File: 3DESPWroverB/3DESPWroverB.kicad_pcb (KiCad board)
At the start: 2 copper layers, 40 x 40 mm, 18 parts, among them J1 Conn_02x07_Odd_Even, J10 Conn_02x03_Odd_Even, J11 Conn_01x01, J12 Conn_01x01, J13 Conn_01x01, J14 Conn_01x01, J15 Conn_01x01, J16 Conn_01x01, J17 Conn_01x01, J18 Conn_01x01, J2 Conn_01x01, J3 Conn_01x01, J4 Conn_01x01, J5 Conn_01x01, J6 Conn_01x01, J7 Conn_01x01, J8 Conn_01x01, J9 Conn_01x01

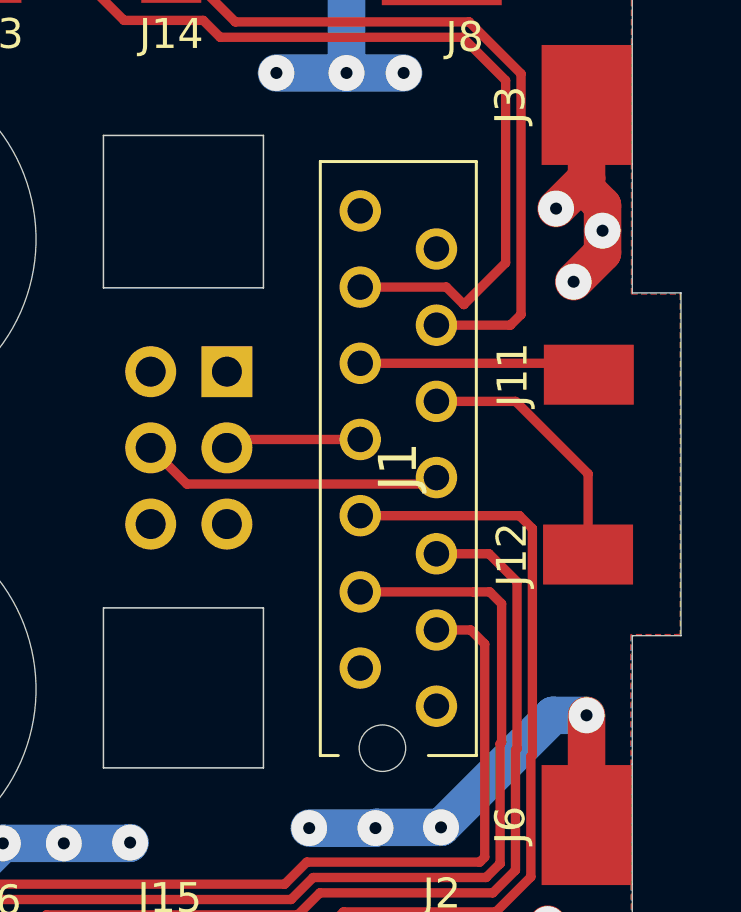
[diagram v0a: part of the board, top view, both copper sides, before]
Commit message: Correction to 3.3v regulator connection
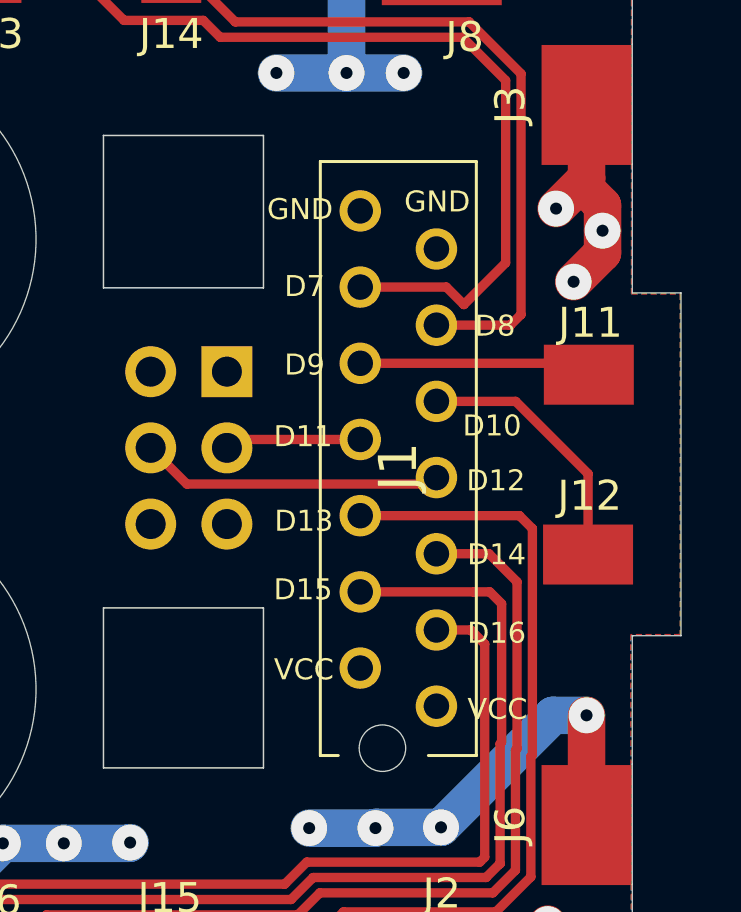
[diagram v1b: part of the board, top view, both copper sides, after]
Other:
- board text added: "D10"
- board text added: "D11"
- board text added: "D12"
- board text added: "D13"
- board text added: "D14"
- board text added: "D15"
- board text added: "D16"
- board text added: "D7"
- board text added: "D8"
- board text added: "D9"
- board text added: "GND"
- board text added: "VCC"
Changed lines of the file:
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@@
   (general
     (thickness 1.6)
-    (drawings 105)
+    (drawings 125)
     (tracks 138)
     (zones 0)
@@
       (effects (font (size 1.27 1.27) (thickness 0.254)))
     )
+    (fp_line (start -1.645 -3.87) (end 18.155 -3.87) (layer F.Fab) (width 0.2))
+    (fp_line (start 18.155 -3.87) (end 18.155 1.33) (layer F.Fab) (width 0.2))
+    (fp_line (start 18.155 1.33) (end -1.645 1.33) (layer F.Fab) (width 0.2))
+    (fp_line (start -1.645 1.33) (end -1.645 -3.87) (layer F.Fab) (width 0.2))
+    (fp_line (start -2.645 -4.87) (end 19.685 -4.87) (layer F.CrtYd) (width 0.1))
+    (fp_line (start 19.685 -4.87) (end 19.685 2.33) (layer F.CrtYd) (width 0.1))
+    (fp_line (start 19.685 2.33) (end -2.645 2.33) (layer F.CrtYd) (width 0.1))
+    (fp_line (start -2.645 2.33) (end -2.645 -4.87) (layer F.CrtYd) (width 0.1))
+    (fp_line (start 18.155 -2.27) (end 18.155 -3.87) (layer F.SilkS) (width 0.1))
+    (fp_line (start 18.155 -3.87) (end -1.645 -3.87) (layer F.SilkS) (width 0.1))
+    (fp_line (start -1.645 -3.87) (end -1.645 1.33) (layer F.SilkS) (width 0.1))
+    (fp_line (start -1.645 1.33) (end 18.155 1.33) (layer F.SilkS) (width 0.1))
     (fp_line (start 18.155 1.33) (end 18.155 0.73) (layer F.SilkS) (width 0.1))
-    (fp_line (start -1.645 1.33) (end 18.155 1.33) (layer F.SilkS) (width 0.1))
-    (fp_line (start -1.645 -3.87) (end -1.645 1.33) (layer F.SilkS) (width 0.1))
-    (fp_line (start 18.155 -3.87) (end -1.645 -3.87) (layer F.SilkS) (width 0.1))
-    (fp_line (start 18.155 -2.27) (end 18.155 -3.87) (layer F.SilkS) (width 0.1))
-    (fp_line (start -2.645 2.33) (end -2.645 -4.87) (layer F.CrtYd) (width 0.1))
-    (fp_line (start 19.685 2.33) (end -2.645 2.33) (layer F.CrtYd) (width 0.1))
-    (fp_line (start 19.685 -4.87) (end 19.685 2.33) (layer F.CrtYd) (width 0.1))
-    (fp_line (start -2.645 -4.87) (end 19.685 -4.87) (layer F.CrtYd) (width 0.1))
-    (fp_line (start -1.645 1.33) (end -1.645 -3.87) (layer F.Fab) (width 0.2))
-    (fp_line (start 18.155 1.33) (end -1.645 1.33) (layer F.Fab) (width 0.2))
-    (fp_line (start 18.155 -3.87) (end 18.155 1.33) (layer F.Fab) (width 0.2))
-    (fp_line (start -1.645 -3.87) (end 18.155 -3.87) (layer F.Fab) (width 0.2))
     (fp_text user %R (at 8.52 -1.27 90) (layer F.Fab)
       (effects (font (size 1.27 1.27) (thickness 0.254)))
@@
   (module Custom:CubeCenterPad (layer F.Cu)
     (at 168.6052 54.4576 270)
-    (fp_text reference J11 (at 0 2.54 90) (layer F.SilkS)
+    (fp_text reference J11 (at -1.7272 -0.0508 180) (layer F.SilkS)
       (effects (font (size 1 1) (thickness 0.15)))
     )
@@
   (module Custom:CubeCenterPad (layer F.Cu)
     (at 168.5798 60.452 270)
-    (fp_text reference J12 (at 0 2.54 90) (layer F.SilkS)
+    (fp_text reference J12 (at -1.9558 -0.0508 180) (layer F.SilkS)
       (effects (font (size 1 1) (thickness 0.15)))
     )
@@
     (descr "Through hole straight pin header, 2x03, 2.54mm pitch, double rows")
     (tags "Through hole pin header THT 2x03 2.54mm double row")
-    (fp_text reference J10 (at 5.2578 -0.8128) (layer B.SilkS)
+    (fp_text reference J10 (at 5.3086 -1.3208) (layer B.SilkS)
       (effects (font (size 1 1) (thickness 0.15)) (justify mirror))
     )
@@
       (effects (font (size 1 1) (thickness 0.15)) (justify mirror))
     )
+    (fp_line (start 0 1.27) (end 3.81 1.27) (layer B.Fab) (width 0.1))
+    (fp_line (start 3.81 1.27) (end 3.81 -6.35) (layer B.Fab) (width 0.1))
+    (fp_line (start 3.81 -6.35) (end -1.27 -6.35) (layer B.Fab) (width 0.1))
+    (fp_line (start -1.27 -6.35) (end -1.27 0) (layer B.Fab) (width 0.1))
+    (fp_line (start -1.27 0) (end 0 1.27) (layer B.Fab) (width 0.1))
+    (fp_line (start -1.33 -6.41) (end 3.87 -6.41) (layer B.SilkS) (width 0.12))
+    (fp_line (start -1.33 -1.27) (end -1.33 -6.41) (layer B.SilkS) (width 0.12))
+    (fp_line (start 3.87 1.33) (end 3.87 -6.41) (layer B.SilkS) (width 0.12))
+    (fp_line (start -1.33 -1.27) (end 1.27 -1.27) (layer B.SilkS) (width 0.12))
+    (fp_line (start 1.27 -1.27) (end 1.27 1.33) (layer B.SilkS) (width 0.12))
+    (fp_line (start 1.27 1.33) (end 3.87 1.33) (layer B.SilkS) (width 0.12))
+    (fp_line (start -1.33 0) (end -1.33 1.33) (layer B.SilkS) (width 0.12))
+    (fp_line (start -1.33 1.33) (end 0 1.33) (layer B.SilkS) (width 0.12))
+    (fp_line (start -1.8 1.8) (end -1.8 -6.85) (layer B.CrtYd) (width 0.05))
+    (fp_line (start -1.8 -6.85) (end 4.35 -6.85) (layer B.CrtYd) (width 0.05))
+    (fp_line (start 4.35 -6.85) (end 4.35 1.8) (layer B.CrtYd) (width 0.05))
     (fp_line (start 4.35 1.8) (end -1.8 1.8) (layer B.CrtYd) (width 0.05))
-    (fp_line (start 4.35 -6.85) (end 4.35 1.8) (layer B.CrtYd) (width 0.05))
-    (fp_line (start -1.8 -6.85) (end 4.35 -6.85) (layer B.CrtYd) (width 0.05))
-    (fp_line (start -1.8 1.8) (end -1.8 -6.85) (layer B.CrtYd) (width 0.05))
-    (fp_line (start -1.33 1.33) (end 0 1.33) (layer B.SilkS) (width 0.12))
-    (fp_line (start -1.33 0) (end -1.33 1.33) (layer B.SilkS) (width 0.12))
-    (fp_line (start 1.27 1.33) (end 3.87 1.33) (layer B.SilkS) (width 0.12))
-    (fp_line (start 1.27 -1.27) (end 1.27 1.33) (layer B.SilkS) (width 0.12))
-    (fp_line (start -1.33 -1.27) (end 1.27 -1.27) (layer B.SilkS) (width 0.12))
-    (fp_line (start 3.87 1.33) (end 3.87 -6.41) (layer B.SilkS) (width 0.12))
-    (fp_line (start -1.33 -1.27) (end -1.33 -6.41) (layer B.SilkS) (width 0.12))
-    (fp_line (start -1.33 -6.41) (end 3.87 -6.41) (layer B.SilkS) (width 0.12))
-    (fp_line (start -1.27 0) (end 0 1.27) (layer B.Fab) (width 0.1))
-    (fp_line (start -1.27 -6.35) (end -1.27 0) (layer B.Fab) (width 0.1))
-    (fp_line (start 3.81 -6.35) (end -1.27 -6.35) (layer B.Fab) (width 0.1))
-    (fp_line (start 3.81 1.27) (end 3.81 -6.35) (layer B.Fab) (width 0.1))
-    (fp_line (start 0 1.27) (end 3.81 1.27) (layer B.Fab) (width 0.1))
     (fp_text user %R (at 1.27 -2.54 270) (layer B.Fab)
       (effects (font (size 1 1) (thickness 0.15)) (justify mirror))
@@
     )
   )
+  (gr_text GND (at 151.5618 54.229 180) (layer B.SilkS)
+    (effects (font (size 0.7 0.7) (thickness 0.15)) (justify mirror))
+  )
+  (gr_text GND (at 163.5506 48.6918) (layer F.SilkS)
+    (effects (font (size 0.7 0.7) (thickness 0.15)))
+  )
+  (gr_text GND (at 158.9786 48.9458) (layer F.SilkS)
+    (effects (font (size 0.7 0.7) (thickness 0.15)))
+  )
+  (gr_text VCC (at 165.5572 65.6082) (layer F.SilkS)
+    (effects (font (size 0.7 0.7) (thickness 0.15)))
+  )
+  (gr_text VCC (at 159.1056 64.2874) (layer F.SilkS)
+    (effects (font (size 0.7 0.7) (thickness 0.15)))
+  )
+  (gr_text D16 (at 165.5318 63.0682) (layer F.SilkS)
+    (effects (font (size 0.7 0.7) (thickness 0.15)))
+  )
+  (gr_text D15 (at 159.0802 61.6204) (layer F.SilkS)
+    (effects (font (size 0.7 0.7) (thickness 0.15)))
+  )
+  (gr_text D14 (at 165.5318 60.452) (layer F.SilkS)
+    (effects (font (size 0.7 0.7) (thickness 0.15)))
+  )
+  (gr_text D13 (at 159.1056 59.3344) (layer F.SilkS)
+    (effects (font (size 0.7 0.7) (thickness 0.15)))
+  )
+  (gr_text D12 (at 165.5064 57.9882) (layer F.SilkS)
+    (effects (font (size 0.7 0.7) (thickness 0.15)))
+  )
+  (gr_text D11 (at 159.0802 56.515) (layer F.SilkS)
+    (effects (font (size 0.7 0.7) (thickness 0.15)))
+  )
+  (gr_text D10 (at 165.3794 56.1594) (layer F.SilkS)
+    (effects (font (size 0.7 0.7) (thickness 0.15)))
+  )
+  (gr_text D9 (at 159.131 54.1274) (layer F.SilkS)
+    (effects (font (size 0.7 0.7) (thickness 0.15)))
+  )
+  (gr_text D8 (at 165.481 52.832) (layer F.SilkS)
+    (effects (font (size 0.7 0.7) (thickness 0.15)))
+  )
+  (gr_text D7 (at 159.131 51.5112) (layer F.SilkS)
+    (effects (font (size 0.7 0.7) (thickness 0.15)))
+  )
+  (gr_text D11 (at 158.7246 56.8452 180) (layer B.SilkS)
+    (effects (font (size 0.7 0.7) (thickness 0.15)) (justify mirror))
+  )
+  (gr_text D12 (at 151.3332 57.023 180) (layer B.SilkS)
+    (effects (font (size 0.7 0.7) (thickness 0.15)) (justify mirror))
+  )
+  (gr_text VCC (at 156.591 61.2648 180) (layer B.SilkS)
+    (effects (font (size 0.7 0.7) (thickness 0.15)) (justify mirror))
+  )
+  (gr_text VCC (at 156.5656 52.4002 180) (layer B.SilkS)
+    (effects (font (size 0.7 0.7) (thickness 0.15)) (justify mirror))
+  )
+  (gr_text GND (at 151.257 59.5884 180) (layer B.SilkS)
+    (effects (font (size 0.7 0.7) (thickness 0.15)) (justify mirror))
+  )
   (gr_text "REAL\nITU\nrodr" (at 151.6888 42.2656) (layer B.SilkS)
     (effects (font (size 1 1) (thickness 0.15)) (justify mirror))
   )
-  (gr_text "Project Cube, v1.1" (at 144.5768 57.4802) (layer B.SilkS)
+  (gr_text "Project Cube, v1.1" (at 142.0114 57.4548) (layer B.SilkS)
     (effects (font (size 1 1) (thickness 0.15)) (justify mirror))
   )

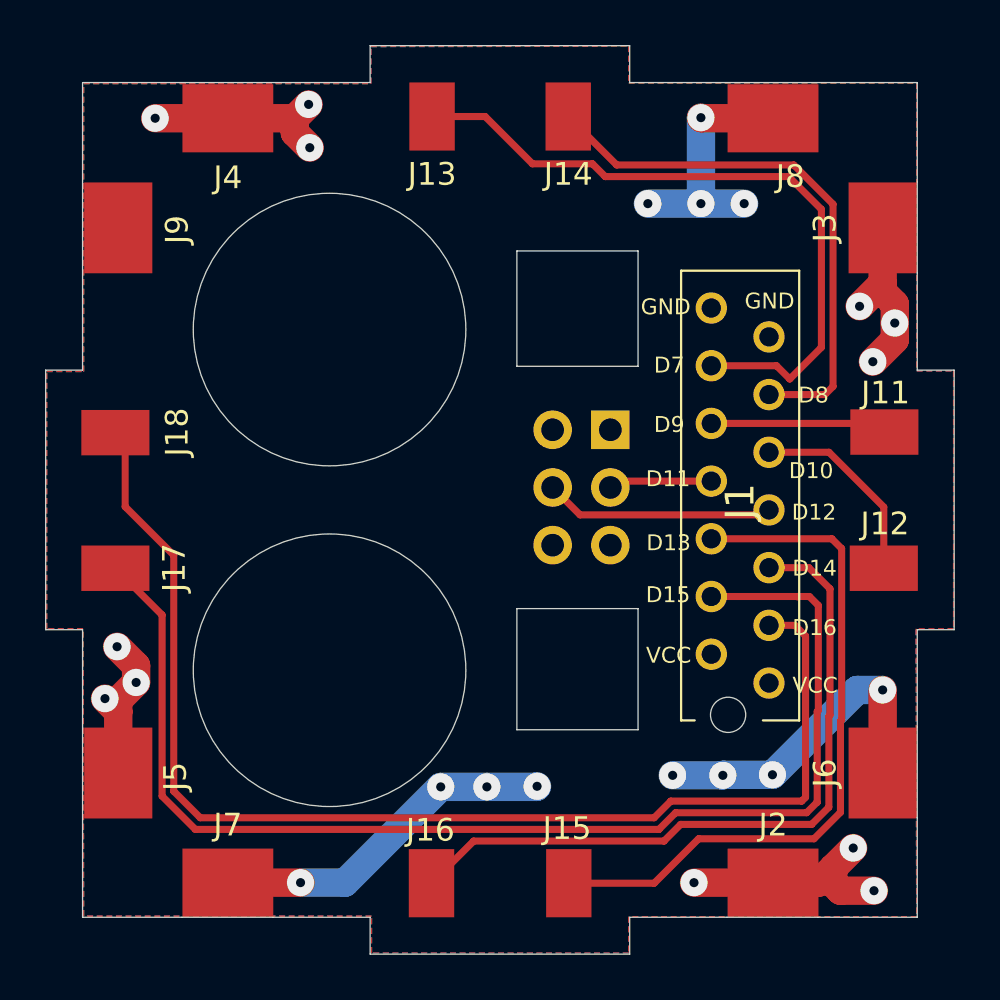
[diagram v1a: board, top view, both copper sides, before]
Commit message: Some components replaced by SMD versions
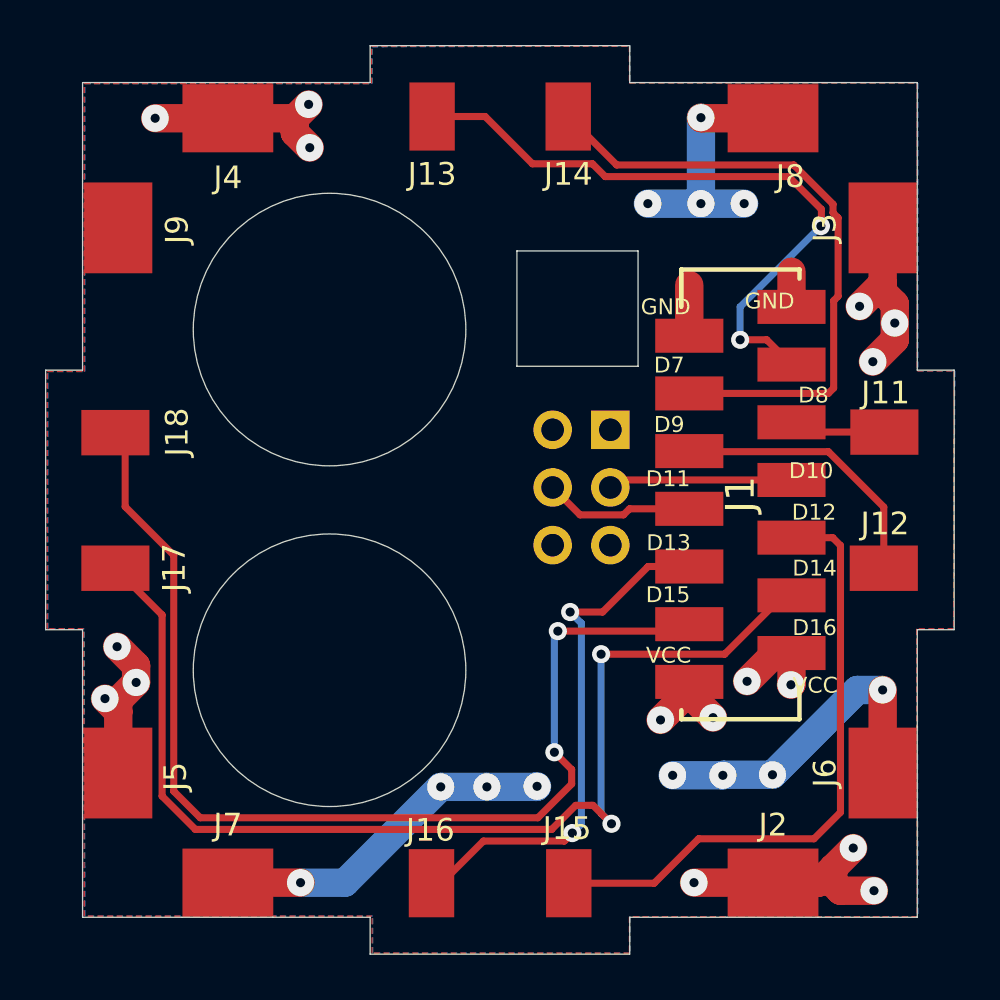
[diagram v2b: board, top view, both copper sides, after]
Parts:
- J1: footprint Custom:TE_Micromatch_2,54_14 -> Custom:TE_Micromatch_2,54_14_SMD
- moved J1 8.30 mm to (162.3, 57.2)
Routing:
- net /D14: track 31.6 -> 23.3 mm, vias 0 -> 2
- net VCC: track 33.8 -> 41.9 mm, vias 12 -> 16
- net /D16: track 54.4 -> 48.5 mm, vias 0 -> 2
- net /D15: track 54.4 -> 49.2 mm, vias 0 -> 2
- net /D11: track 4.56 -> 8.51 mm
- net GND: track 41.0 -> 44.8 mm
- net /D8: track 24.3 -> 28.0 mm
- net /D10: track 8.75 -> 12.3 mm
- net /D13: track 30.8 -> 27.3 mm
- net /D12: track 10.1 -> 6.63 mm
- net /D9: track 7.78 -> 4.81 mm
- net /D7: track 30.6 -> 28.8 mm, vias 0 -> 2
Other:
- outline, holes or cut-outs redrawn
